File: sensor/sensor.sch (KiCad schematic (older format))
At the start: 27 parts, among them IC1 AD5933YRSZ, IC2 MAX86141ENP+T, J1 502078-1710, J2 Probe_01_male, J3 Probe_01_male, J4 Probe_01_male, J5 Probe_01_male

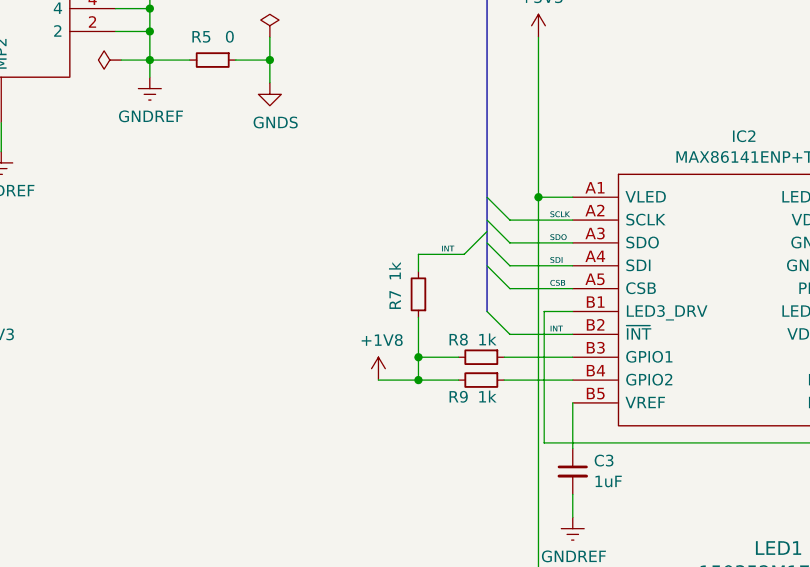
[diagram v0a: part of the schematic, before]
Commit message: fix resistor type at BOM changed from 0402 to 1005 metric size
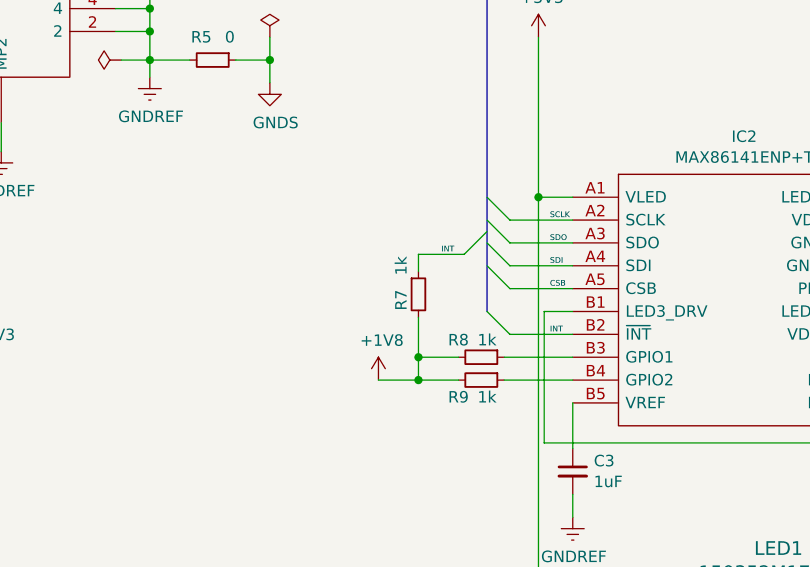
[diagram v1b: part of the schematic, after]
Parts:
- R3, R4: Digikey Part Number 541-4276-2-ND -> 541-3959-2-ND; Manufacturer Part Number CRCW010010K0JREL -> CRCW040210K0FKEDC; Mouser Price/Stock https://www.mouser.ee/ProductDetail/Vishay-Dale/CRCW010010K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 -> https://www.mouser.ee/ProductDetail/Vishay-Dale/CRCW040210K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; Price 0.14 -> 0.09
- R6, R7, R8, R9: Digikey Part Number 541-4279-2-ND -> 541-3961-2-ND; Manufacturer Part Number CRCW01001K00JREL -> CRCW04021K00FKEDC; Mouser Price/Stock https://www.mouser.ee/ProductDetail/Vishay-Dale/CRCW01001K0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 -> https://www.mouser.ee/ProductDetail/Vishay-Dale/CRCW04021K0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; Price 0.14 -> 0.09
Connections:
- net +1V8: now also R7.2; no longer R7.1
- net INT: now also R7.1; no longer R7.2
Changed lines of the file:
@@
 F 1 "1k" V 4175 3675 50  0000 C CNN
 F 2 "Resistor_SMD:R_0402_1005Metric" H 4250 3650 50  0001 C CNN
-F 3 "https://www.mouser.ee/datasheet/2/427/crcw01005e3-1762154.pdf" H 4250 3650 50  0001 C CNN
+F 3 "https://www.mouser.ee/datasheet/2/427/crcwce3-1762584.pdf" H 4250 3650 50  0001 C CNN
 F 4 "Vishay / Dale" V 4250 3650 50  0001 C CNN "Manufacturer"
-F 5 "CRCW01001K00JREL" V 4250 3650 50  0001 C CNN "Manufacturer Part Number"
-F 6 "https://www.mouser.ee/ProductDetail/Vishay-Dale/CRCW01001K00JREL/?qs=sGAEpiMZZMvdGkrng054txORKzL4v1djRk1beXIIrRMZVMBzjQ6U%252BQ%3D%3D" V 4250 3650 50  0001 C CNN "Mouser Price/Stock"
-F 7 "541-4279-2-ND" V 4250 3650 50  0001 C CNN "Digikey Part Number"
-F 8 "0.14" V 4250 3650 50  0001 C CNN "Price"
+F 5 "CRCW04021K00FKEDC" V 4250 3650 50  0001 C CNN "Manufacturer Part Number"
+F 6 "https://www.mouser.ee/ProductDetail/Vishay-Dale/CRCW04021K00FKEDC?qs=sGAEpiMZZMvdGkrng054t8r8AhKhXLMm3e8cE5j2FQOWYLX7Ezsnvg%3D%3D" V 4250 3650 50  0001 C CNN "Mouser Price/Stock"
+F 7 "541-3961-2-ND" V 4250 3650 50  0001 C CNN "Digikey Part Number"
+F 8 "0.09" V 4250 3650 50  0001 C CNN "Price"
 	1    4250 3650
 	0    1    1    0
@@
 Text Label 4550 3550 0    25   ~ 0
 INT
-$Comp
-L Device:R_Small R7
-U 1 1 5FEA19E0
-P 3975 3375
-F 0 "R7" V 4075 3400 50  0000 C CNN
-F 1 "1k" V 4075 3275 50  0000 C CNN
-F 2 "Resistor_SMD:R_0402_1005Metric" H 3975 3375 50  0001 C CNN
-F 3 "https://www.mouser.ee/datasheet/2/427/crcw01005e3-1762154.pdf" H 3975 3375 50  0001 C CNN
-F 4 "Vishay / Dale" V 3975 3375 50  0001 C CNN "Manufacturer"
-F 5 "CRCW01001K00JREL" V 3975 3375 50  0001 C CNN "Manufacturer Part Number"
-F 6 "https://www.mouser.ee/ProductDetail/Vishay-Dale/CRCW01001K00JREL/?qs=3CaSHoNeR5tPjJyYZZWXXA%3D%3D" V 3975 3375 50  0001 C CNN "Mouser Price/Stock"
-F 7 "541-4279-2-ND" V 3975 3375 50  0001 C CNN "Digikey Part Number"
-F 8 "0.14" V 3975 3375 50  0001 C CNN "Price"
-	1    3975 3375
-	-1   0    0    1
-$EndComp
 Connection ~ 3975 3650
-$Comp
-L Device:R_Small R9
-U 1 1 5FEEC142
-P 4250 3750
-F 0 "R9" V 4325 3650 50  0000 C CNN
-F 1 "1k" V 4325 3775 50  0000 C CNN
-F 2 "Resistor_SMD:R_0402_1005Metric" H 4250 3750 50  0001 C CNN
-F 3 "https://www.mouser.ee/datasheet/2/427/crcw01005e3-1762154.pdf" H 4250 3750 50  0001 C CNN
-F 4 "Vishay / Dale" V 4250 3750 50  0001 C CNN "Manufacturer"
-F 5 "CRCW01001K00JREL" V 4250 3750 50  0001 C CNN "Manufacturer Part Number"
-F 6 "https://www.mouser.ee/ProductDetail/Vishay-Dale/CRCW01001K00JREL/?qs=sGAEpiMZZMvdGkrng054txORKzL4v1djRk1beXIIrRMZVMBzjQ6U%252BQ%3D%3D" V 4250 3750 50  0001 C CNN "Mouser Price/Stock"
-F 7 "541-4279-2-ND" V 4250 3750 50  0001 C CNN "Digikey Part Number"
-F 8 "0.14" V 4250 3750 50  0001 C CNN "Price"
-	1    4250 3750
-	0    1    1    0
-$EndComp
 Wire Wire Line
 	4375 3550 4650 3550
@@
 Entry Wire Line
 	1275 3825 1375 3925
-$Comp
-L Device:R_Small R4
-U 1 1 5FFE0EE1
-P 1675 3925
-F 0 "R4" V 1750 3825 50  0000 C CNN
-F 1 "10k" V 1750 3975 50  0000 C CNN
-F 2 "Resistor_SMD:R_0402_1005Metric" H 1675 3925 50  0001 C CNN
-F 3 "https://www.mouser.ee/datasheet/2/427/crcw01005e3-1762154.pdf" H 1675 3925 50  0001 C CNN
-F 4 "Vishay / Dale" V 1675 3925 50  0001 C CNN "Manufacturer"
-F 5 "CRCW010010K0JREL" V 1675 3925 50  0001 C CNN "Manufacturer Part Number"
-F 6 "https://www.mouser.ee/ProductDetail/Vishay-Dale/CRCW010010K0JREL/?qs=sGAEpiMZZMvdGkrng054txORKzL4v1dj6%252BCtVKBihJgYoUo1WvZr%252BA%3D%3D" V 1675 3925 50  0001 C CNN "Mouser Price/Stock"
-F 7 "541-4276-2-ND" V 1675 3925 50  0001 C CNN "Digikey Part Number"
-F 8 "0.14" V 1675 3925 50  0001 C CNN "Price"
-	1    1675 3925
-	0    1    1    0
-$EndComp
 Wire Wire Line
 	1375 3925 1575 3925
@@
 Wire Wire Line
 	2100 3725 2100 3825
-$Comp
-L Device:R_Small R6
-U 1 1 600093C1
-P 3300 6025
-F 0 "R6" V 3375 5925 50  0000 C CNN
-F 1 "1k" V 3375 6050 50  0000 C CNN
-F 2 "Resistor_SMD:R_0402_1005Metric" H 3300 6025 50  0001 C CNN
-F 3 "https://www.mouser.ee/datasheet/2/427/crcw01005e3-1762154.pdf" H 3300 6025 50  0001 C CNN
-F 4 "Vishay / Dale" V 3300 6025 50  0001 C CNN "Manufacturer"
-F 5 "CRCW01001K00JREL" V 3300 6025 50  0001 C CNN "Manufacturer Part Number"
-F 6 "https://www.mouser.ee/ProductDetail/Vishay-Dale/CRCW01001K00JREL/?qs=sGAEpiMZZMvdGkrng054txORKzL4v1djRk1beXIIrRMZVMBzjQ6U%252BQ%3D%3D" V 3300 6025 50  0001 C CNN "Mouser Price/Stock"
-F 7 "541-4279-2-ND" V 3300 6025 50  0001 C CNN "Digikey Part Number"
-F 8 "0.14" V 3300 6025 50  0001 C CNN "Price"
-	1    3300 6025
-	0    1    1    0
-$EndComp
 $Comp
 L Device:C_Small C2
@@
 F 1 "10k" V 1600 3875 50  0000 C CNN
 F 2 "Resistor_SMD:R_0402_1005Metric" H 1675 3825 50  0001 C CNN
-F 3 "https://www.mouser.ee/datasheet/2/427/crcw01005e3-1762154.pdf" H 1675 3825 50  0001 C CNN
+F 3 "https://www.mouser.ee/datasheet/2/427/crcwce3-1762584.pdf" H 1675 3825 50  0001 C CNN
 F 4 "Vishay / Dale" V 1675 3825 50  0001 C CNN "Manufacturer"
-F 5 "CRCW010010K0JREL" V 1675 3825 50  0001 C CNN "Manufacturer Part Number"
-F 6 "https://www.mouser.ee/ProductDetail/Vishay-Dale/CRCW010010K0JREL/?qs=sGAEpiMZZMvdGkrng054txORKzL4v1dj6%252BCtVKBihJgYoUo1WvZr%252BA%3D%3D" V 1675 3825 50  0001 C CNN "Mouser Price/Stock"
-F 7 "541-4276-2-ND" V 1675 3825 50  0001 C CNN "Digikey Part Number"
-F 8 "0.14" V 1675 3825 50  0001 C CNN "Price"
+F 5 "CRCW040210K0FKEDC" V 1675 3825 50  0001 C CNN "Manufacturer Part Number"
+F 6 "https://www.mouser.ee/ProductDetail/Vishay-Dale/CRCW040210K0FKEDC?qs=sGAEpiMZZMvdGkrng054t8r8AhKhXLMmRzRvL6rLfpm%252B44%252BFlSmM9Q%3D%3D" V 1675 3825 50  0001 C CNN "Mouser Price/Stock"
+F 7 "541-3959-2-ND" V 1675 3825 50  0001 C CNN "Digikey Part Number"
+F 8 "0.09" V 1675 3825 50  0001 C CNN "Price"
 	1    1675 3825
 	0    1    1    0
@@
 	0    1    1    0
 $EndComp
+$Comp
+L Device:R_Small R9
+U 1 1 6088400C
+P 4250 3750
+F 0 "R9" V 4325 3650 50  0000 C CNN
+F 1 "1k" V 4325 3775 50  0000 C CNN
+F 2 "Resistor_SMD:R_0402_1005Metric" H 4250 3750 50  0001 C CNN
+F 3 "https://www.mouser.ee/datasheet/2/427/crcwce3-1762584.pdf" H 4250 3750 50  0001 C CNN
+F 4 "Vishay / Dale" V 4250 3750 50  0001 C CNN "Manufacturer"
+F 5 "CRCW04021K00FKEDC" V 4250 3750 50  0001 C CNN "Manufacturer Part Number"
+F 6 "https://www.mouser.ee/ProductDetail/Vishay-Dale/CRCW04021K00FKEDC?qs=sGAEpiMZZMvdGkrng054t8r8AhKhXLMm3e8cE5j2FQOWYLX7Ezsnvg%3D%3D" V 4250 3750 50  0001 C CNN "Mouser Price/Stock"
+F 7 "541-3961-2-ND" V 4250 3750 50  0001 C CNN "Digikey Part Number"
+F 8 "0.09" V 4250 3750 50  0001 C CNN "Price"
+	1    4250 3750
+	0    1    1    0
+$EndComp
+$Comp
+L Device:R_Small R6
+U 1 1 6088E93B
+P 3300 6025
+F 0 "R6" V 3375 5925 50  0000 C CNN
+F 1 "1k" V 3375 6050 50  0000 C CNN
+F 2 "Resistor_SMD:R_0402_1005Metric" H 3300 6025 50  0001 C CNN
+F 3 "https://www.mouser.ee/datasheet/2/427/crcwce3-1762584.pdf" H 3300 6025 50  0001 C CNN
+F 4 "Vishay / Dale" V 3300 6025 50  0001 C CNN "Manufacturer"
+F 5 "CRCW04021K00FKEDC" V 3300 6025 50  0001 C CNN "Manufacturer Part Number"
+F 6 "https://www.mouser.ee/ProductDetail/Vishay-Dale/CRCW04021K00FKEDC?qs=sGAEpiMZZMvdGkrng054t8r8AhKhXLMm3e8cE5j2FQOWYLX7Ezsnvg%3D%3D" V 3300 6025 50  0001 C CNN "Mouser Price/Stock"
+F 7 "541-3961-2-ND" V 3300 6025 50  0001 C CNN "Digikey Part Number"
+F 8 "0.09" V 3300 6025 50  0001 C CNN "Price"
+	1    3300 6025
+	0    1    1    0
+$EndComp
+$Comp
+L Device:R_Small R7
+U 1 1 60898C47
+P 3975 3375
+F 0 "R7" V 3900 3350 50  0000 C CNN
+F 1 "1k" V 3900 3500 50  0000 C CNN
+F 2 "Resistor_SMD:R_0402_1005Metric" H 3975 3375 50  0001 C CNN
+F 3 "https://www.mouser.ee/datasheet/2/427/crcwce3-1762584.pdf" H 3975 3375 50  0001 C CNN
+F 4 "Vishay / Dale" V 3975 3375 50  0001 C CNN "Manufacturer"
+F 5 "CRCW04021K00FKEDC" V 3975 3375 50  0001 C CNN "Manufacturer Part Number"
+F 6 "https://www.mouser.ee/ProductDetail/Vishay-Dale/CRCW04021K00FKEDC?qs=sGAEpiMZZMvdGkrng054t8r8AhKhXLMm3e8cE5j2FQOWYLX7Ezsnvg%3D%3D" V 3975 3375 50  0001 C CNN "Mouser Price/Stock"
+F 7 "541-3961-2-ND" V 3975 3375 50  0001 C CNN "Digikey Part Number"
+F 8 "0.09" V 3975 3375 50  0001 C CNN "Price"
+	1    3975 3375
+	1    0    0    -1
+$EndComp
 Wire Bus Line
 	1275 3725 1275 6225
@@
 Wire Bus Line
 	4275 900  4275 3450
+$Comp
+L Device:R_Small R4
+U 1 1 608A2FDA
+P 1675 3925
+F 0 "R4" V 1750 3825 50  0000 C CNN
+F 1 "10k" V 1750 3975 50  0000 C CNN
+F 2 "Resistor_SMD:R_0402_1005Metric" H 1675 3925 50  0001 C CNN
+F 3 "https://www.mouser.ee/datasheet/2/427/crcwce3-1762584.pdf" H 1675 3925 50  0001 C CNN
+F 4 "Vishay / Dale" V 1675 3925 50  0001 C CNN "Manufacturer"
+F 5 "CRCW040210K0FKEDC" V 1675 3925 50  0001 C CNN "Manufacturer Part Number"
+F 6 "https://www.mouser.ee/ProductDetail/Vishay-Dale/CRCW040210K0FKEDC?qs=sGAEpiMZZMvdGkrng054t8r8AhKhXLMmRzRvL6rLfpm%252B44%252BFlSmM9Q%3D%3D" V 1675 3925 50  0001 C CNN "Mouser Price/Stock"
+F 7 "541-3959-2-ND" V 1675 3925 50  0001 C CNN "Digikey Part Number"
+F 8 "0.09" V 1675 3925 50  0001 C CNN "Price"
+	1    1675 3925
+	0    1    1    0
+$EndComp
 $EndSCHEMATC
